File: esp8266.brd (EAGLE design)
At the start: 29.5 x 28.6 mm, 35 parts, among them IC1 74LVC1G08DBV, U1 FT232RL-BASICSSOP, U2 SPX3819M5-L33

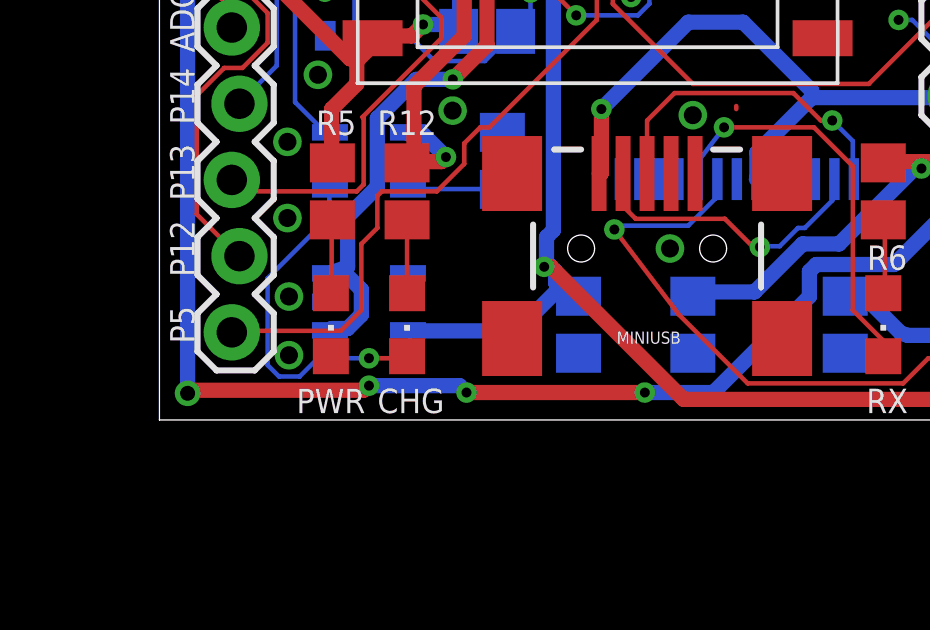
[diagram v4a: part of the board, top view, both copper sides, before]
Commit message: Even less wires and 3 unnecessary vias.
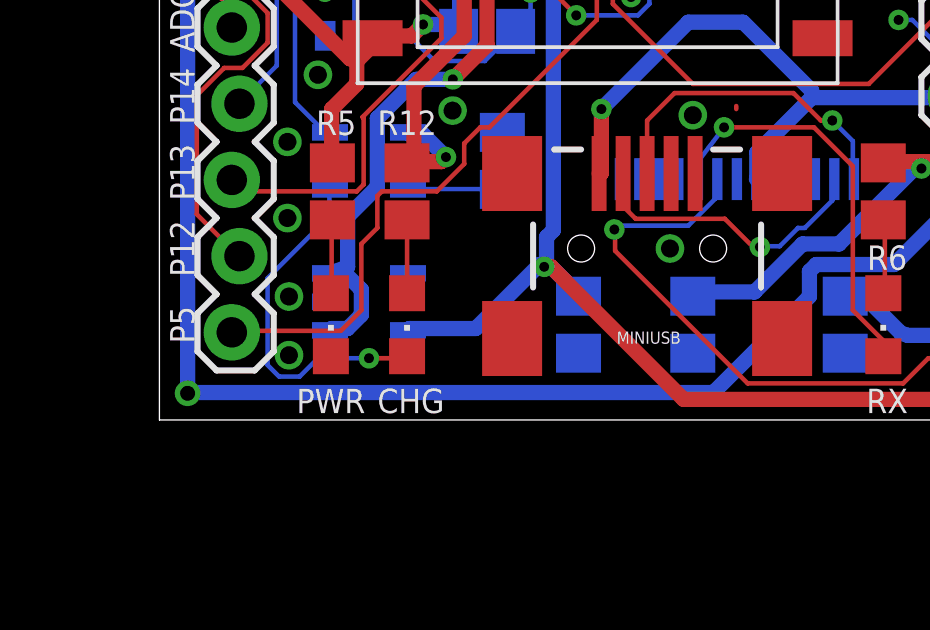
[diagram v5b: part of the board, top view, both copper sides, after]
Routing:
- net VIN: track 73.0 -> 72.8 mm, vias 6 -> 3
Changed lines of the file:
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@@
 <wire x1="11.5062" y1="71.7042" x2="11.5062" y2="72.0852" width="0.508" layer="1"/>
 <wire x1="9.906" y1="70.104" x2="11.5062" y2="71.7042" width="0.508" layer="1"/>
-<wire x1="19.1262" y1="52.3494" x2="18.8976" y2="52.578" width="0.508" layer="16"/>
-<wire x1="25.0698" y1="52.3494" x2="19.1262" y2="52.3494" width="0.508" layer="1"/>
-<wire x1="27.3558" y1="52.3494" x2="25.0698" y2="52.3494" width="0.508" layer="16"/>
 <wire x1="30.5562" y1="55.5498" x2="27.3558" y2="52.3494" width="0.508" layer="16"/>
 <wire x1="30.5562" y1="56.388" x2="30.5562" y2="55.5498" width="0.508" layer="16"/>
@@
 <wire x1="35.2044" y1="58.4454" x2="35.433" y2="58.538" width="0.508" layer="16"/>
 <via x="9.906" y="68.453" extent="1-16" drill="0.3302"/>
-<via x="15.875" y="52.578" extent="1-16" drill="0.3302"/>
-<via x="19.1262" y="52.3494" extent="1-16" drill="0.3302"/>
-<via x="25.0698" y="52.3494" extent="1-16" drill="0.3302"/>
 <via x="9.8298" y="52.324" extent="1-16" drill="0.5"/>
-<wire x1="9.8298" y1="52.3494" x2="9.8298" y2="52.324" width="0.508" layer="1"/>
 <wire x1="9.8298" y1="65.6082" x2="9.8298" y2="52.324" width="0.508" layer="16"/>
-<wire x1="10.0584" y1="52.4256" x2="15.6972" y2="52.4256" width="0.508" layer="1"/>
-<wire x1="15.6972" y1="52.4256" x2="15.875" y2="52.578" width="0.508" layer="1"/>
-<wire x1="10.0584" y1="52.4256" x2="9.8298" y2="52.324" width="0.508" layer="1"/>
-<wire x1="18.8976" y1="52.578" x2="15.875" y2="52.578" width="0.508" layer="16"/>
 <wire x1="9.906" y1="70.104" x2="9.906" y2="68.453" width="0.508" layer="1"/>
 <wire x1="9.906" y1="65.8368" x2="9.906" y2="68.453" width="0.508" layer="16"/>
 <wire x1="9.906" y1="65.8368" x2="9.8298" y2="65.6082" width="0.508" layer="16"/>
+<wire x1="27.3558" y1="52.3494" x2="10.0584" y2="52.3494" width="0.508" layer="16"/>
+<wire x1="10.0584" y1="52.3494" x2="9.8298" y2="52.324" width="0.508" layer="16"/>
 </signal>
 <signal name="DTR">
@@
 <wire x1="14.6304" y1="60.0456" x2="14.6558" y2="60.005" width="0.508" layer="1"/>
 <wire x1="15.9258" y1="64.0842" x2="15.995" y2="64.16" width="0.508" layer="1"/>
-<wire x1="20.955" y1="54.4068" x2="17.2212" y2="54.4068" width="0.508" layer="16"/>
-<wire x1="17.2212" y1="54.4068" x2="17.1751" y2="54.422" width="0.508" layer="16"/>
 <wire x1="22.0218" y1="57.7596" x2="22.0218" y2="67.1322" width="0.508" layer="16"/>
 <wire x1="21.7932" y1="57.531" x2="22.0218" y2="57.7596" width="0.508" layer="16"/>
@@
 <wire x1="34.29" y1="59.817" x2="34.29" y2="60.0456" width="0.508" layer="1"/>
 <wire x1="26.8986" y1="55.7022" x2="26.67" y2="55.56" width="0.508" layer="16"/>
-<wire x1="21.0312" y1="54.6354" x2="22.1742" y2="55.7784" width="0.508" layer="16"/>
-<wire x1="21.0312" y1="54.6354" x2="20.955" y2="54.4068" width="0.508" layer="16"/>
 <via x="34.29" y="59.817" extent="1-16" drill="0.3302"/>
-<wire x1="22.3266" y1="55.626" x2="22.86" y2="55.626" width="0.508" layer="16"/>
-<wire x1="22.86" y1="55.626" x2="22.86" y2="55.56" width="0.508" layer="16"/>
-<wire x1="22.3266" y1="55.626" x2="22.1742" y2="55.7784" width="0.508" layer="16"/>
-<wire x1="22.098" y1="56.388" x2="22.098" y2="56.007" width="0.508" layer="16"/>
-<wire x1="21.7932" y1="56.6928" x2="21.8313" y2="56.6547" width="0.508" layer="16"/>
-<wire x1="21.8313" y1="56.6547" x2="22.098" y2="56.388" width="0.508" layer="16"/>
 <wire x1="21.7932" y1="57.531" x2="21.7932" y2="56.6928" width="0.508" layer="16"/>
-<wire x1="22.098" y1="56.007" x2="22.1742" y2="55.7784" width="0.508" layer="16"/>
 <wire x1="21.9456" y1="56.5404" x2="21.717" y2="56.5404" width="0.508" layer="1"/>
 <wire x1="26.3652" y1="52.1208" x2="21.9456" y2="56.5404" width="0.508" layer="1"/>
@@
 <wire x1="36.7284" y1="59.055" x2="36.7284" y2="52.8828" width="0.508" layer="1"/>
 <wire x1="35.814" y1="59.9694" x2="36.7284" y2="59.055" width="0.508" layer="1"/>
-<wire x1="21.717" y1="56.5404" x2="21.8313" y2="56.6547" width="0.508" layer="16"/>
 <wire x1="35.814" y1="59.9694" x2="35.56" y2="60.005" width="0.508" layer="1"/>
 <via x="21.717" y="56.5404" extent="1-16" drill="0.3302"/>
@@
 <wire x1="18.8976" y1="66.9036" x2="16.383" y2="66.9036" width="0.508" layer="16"/>
 <wire x1="16.383" y1="66.9036" x2="16.317" y2="66.832" width="0.508" layer="16"/>
+<wire x1="19.431" y1="54.483" x2="17.2212" y2="54.483" width="0.508" layer="16"/>
+<wire x1="21.5646" y1="56.6166" x2="19.431" y2="54.483" width="0.508" layer="16"/>
+<wire x1="17.2212" y1="54.483" x2="17.1751" y2="54.422" width="0.508" layer="16"/>
+<wire x1="21.5646" y1="56.6166" x2="21.717" y2="56.5404" width="0.508" layer="16"/>
+<wire x1="21.9456" y1="56.5404" x2="22.86" y2="55.626" width="0.508" layer="16"/>
+<wire x1="22.86" y1="55.626" x2="22.86" y2="55.56" width="0.508" layer="16"/>
+<wire x1="21.9456" y1="56.5404" x2="21.717" y2="56.5404" width="0.508" layer="16"/>
+<wire x1="21.717" y1="56.5404" x2="21.7932" y2="56.6928" width="0.508" layer="16"/>
 </signal>
 <signal name="RXLED">
@@
 <wire x1="33.6804" y1="52.6542" x2="34.5186" y2="53.4924" width="0.1524" layer="1"/>
 <wire x1="28.4988" y1="52.6542" x2="33.6804" y2="52.6542" width="0.1524" layer="1"/>
-<wire x1="26.2128" y1="54.9402" x2="28.4988" y2="52.6542" width="0.1524" layer="1"/>
-<wire x1="24.0538" y1="57.785" x2="26.2128" y2="54.9402" width="0.1524" layer="1"/>
 <wire x1="35.5092" y1="53.4924" x2="35.56" y2="53.56" width="0.1524" layer="1"/>
 <wire x1="27.432" y1="59.436" x2="27.488" y2="59.463" width="0.1524" layer="16"/>
@@
 <wire x1="27.432" y1="58.8264" x2="27.488" y2="59.463" width="0.1524" layer="16"/>
 <wire x1="24.0792" y1="57.8358" x2="24.0538" y2="57.785" width="0.1524" layer="16"/>
+<wire x1="24.0792" y1="57.0738" x2="24.0792" y2="57.7596" width="0.1524" layer="1"/>
+<wire x1="28.4988" y1="52.6542" x2="24.0792" y2="57.0738" width="0.1524" layer="1"/>
+<wire x1="24.0792" y1="57.7596" x2="24.0538" y2="57.785" width="0.1524" layer="1"/>
 </signal>
 <signal name="TXLED">
@@
 <wire x1="32.004" y1="59.5122" x2="32.038" y2="59.463" width="0.1524" layer="16"/>
 <via x="31.3182" y="61.4172" extent="1-16" drill="0.3302"/>
+<wire x1="25.146" y1="61.4172" x2="26.0604" y2="62.3316" width="0.1524" layer="1"/>
+<wire x1="25.146" y1="61.4172" x2="25.146" y2="59.65" width="0.1524" layer="1"/>
 <wire x1="30.9372" y1="61.4172" x2="31.3182" y2="61.4172" width="0.1524" layer="1"/>
 <wire x1="30.0228" y1="62.3316" x2="30.9372" y2="61.4172" width="0.1524" layer="1"/>
 <wire x1="26.0604" y1="62.3316" x2="30.0228" y2="62.3316" width="0.1524" layer="1"/>
-<wire x1="25.146" y1="61.4172" x2="26.0604" y2="62.3316" width="0.1524" layer="1"/>
-<wire x1="25.146" y1="61.4172" x2="25.146" y2="59.65" width="0.1524" layer="1"/>
 </signal>
 <signal name="N$6">

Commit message: I kinda need to stop doing this…
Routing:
- net GND: track 75.1 -> 53.9 mm
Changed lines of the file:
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@@
 <wire x1="28.6512" y1="70.4342" x2="29.4132" y2="68.5038" width="0.1524" layer="16"/>
 <wire x1="30.0228" y1="71.1708" x2="28.6512" y2="70.4342" width="0.1524" layer="1"/>
-<wire x1="35.8902" y1="71.1708" x2="30.0228" y2="71.1708" width="0.1524" layer="1"/>
-<wire x1="36.957" y1="72.2376" x2="35.8902" y2="71.1708" width="0.1524" layer="1"/>
-<wire x1="36.957" y1="78.105" x2="36.957" y2="72.2376" width="0.1524" layer="1"/>
 <wire x1="36.0426" y1="79.0194" x2="36.957" y2="78.105" width="0.1524" layer="1"/>
 <wire x1="29.8704" y1="79.0194" x2="36.0426" y2="79.0194" width="0.1524" layer="1"/>
@@
 <wire x1="15.1638" y1="72.9996" x2="14.7066" y2="73.4568" width="0.1524" layer="1"/>
 <wire x1="17.145" y1="72.9996" x2="15.1638" y2="72.9996" width="0.1524" layer="1"/>
-<wire x1="17.2974" y1="72.8472" x2="17.145" y2="72.9996" width="0.1524" layer="1"/>
-<wire x1="17.2974" y1="67.5132" x2="17.2974" y2="72.8472" width="0.1524" layer="1"/>
 <wire x1="16.8402" y1="67.056" x2="17.2974" y2="67.5132" width="0.1524" layer="1"/>
 <wire x1="14.9352" y1="67.056" x2="16.8402" y2="67.056" width="0.1524" layer="1"/>
@@
 <wire x1="35.2044" y1="63.5508" x2="33.9852" y2="64.77" width="0.1524" layer="16"/>
 <wire x1="36.957" y1="64.3128" x2="36.195" y2="63.5508" width="0.1524" layer="16"/>
-<wire x1="36.957" y1="66.04" x2="36.957" y2="64.3128" width="0.1524" layer="16"/>
-<wire x1="36.957" y1="66.675" x2="36.957" y2="66.04" width="0.1524" layer="1"/>
 <wire x1="37.5666" y1="67.2846" x2="36.957" y2="66.675" width="0.1524" layer="1"/>
 <wire x1="37.5666" y1="69.6468" x2="37.5666" y2="67.2846" width="0.1524" layer="1"/>
@@
 <wire x1="34.0106" y1="71.0438" x2="34.7472" y2="71.0184" width="0.1524" layer="1"/>
 <via x="33.528" y="64.77" extent="1-16" drill="0.3302"/>
-<via x="36.957" y="66.04" extent="1-16" drill="0.3302"/>
+<via x="36.703" y="63.373" extent="1-16" drill="0.3302"/>
 <via x="34.0106" y="71.0438" extent="1-16" drill="0.3302"/>
 <wire x1="28.1178" y1="61.7982" x2="28.1178" y2="61.8998" width="0.1524" layer="1"/>
@@
 <wire x1="11.5062" y1="72.0852" x2="11.557" y2="72.136" width="0.508" layer="1"/>
 <wire x1="35.2044" y1="58.4454" x2="35.433" y2="58.538" width="0.508" layer="16"/>
-<via x="9.906" y="68.453" extent="1-16" drill="0.3302"/>
+<via x="9.9822" y="68.453" extent="1-16" drill="0.3302"/>
 <via x="9.8298" y="52.324" extent="1-16" drill="0.5"/>
 <wire x1="9.8298" y1="65.6082" x2="9.8298" y2="52.324" width="0.508" layer="16"/>
-<wire x1="9.906" y1="70.104" x2="9.906" y2="68.453" width="0.508" layer="1"/>
-<wire x1="9.906" y1="65.8368" x2="9.906" y2="68.453" width="0.508" layer="16"/>
+<wire x1="9.906" y1="70.104" x2="9.9822" y2="68.453" width="0.508" layer="1"/>
+<wire x1="9.906" y1="65.8368" x2="9.9822" y2="68.453" width="0.508" layer="16"/>
 <wire x1="9.906" y1="65.8368" x2="9.8298" y2="65.6082" width="0.508" layer="16"/>
 <wire x1="27.3558" y1="52.3494" x2="10.0584" y2="52.3494" width="0.508" layer="16"/>

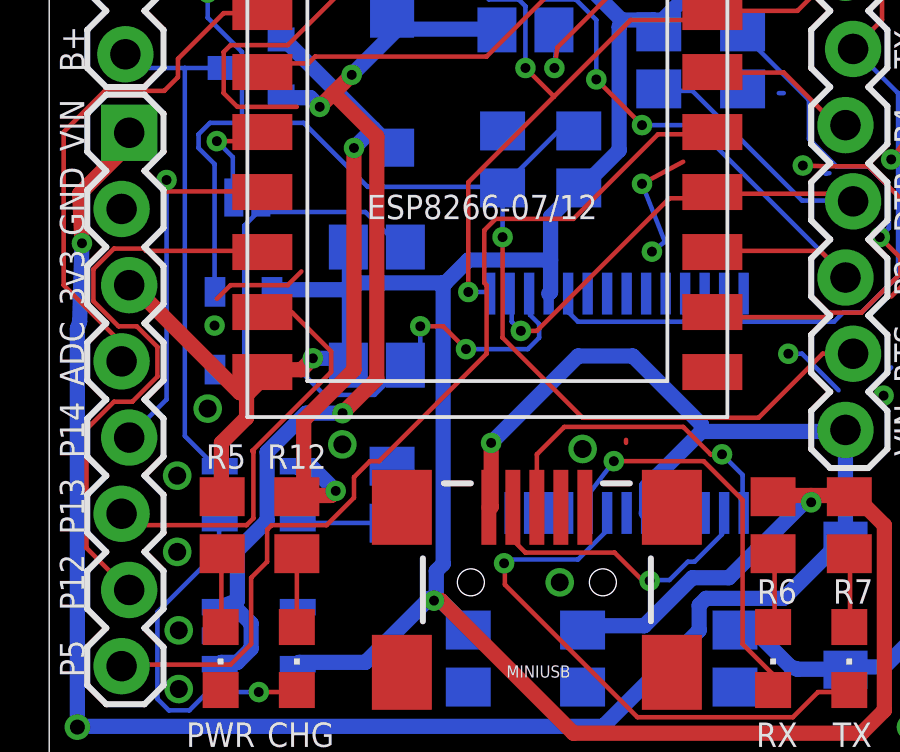
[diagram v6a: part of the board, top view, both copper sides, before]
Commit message: Improve the clarity of the FDTI orientation
This was accomplish by moving the via a to a higher position so that it doesn't interfere with the markings.
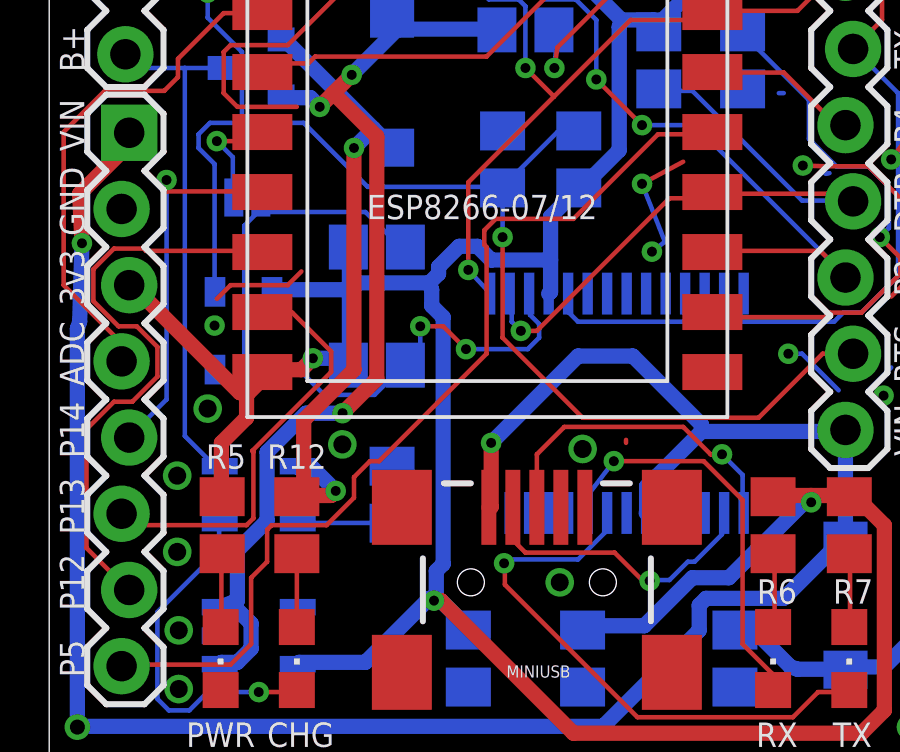
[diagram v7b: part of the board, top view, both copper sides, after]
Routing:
- net 3V3: track 100.1 -> 100.8 mm
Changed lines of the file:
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@@
 <grid distance="0.025" unitdist="inch" unit="inch" style="dots" multiple="1" display="no" altdistance="0.01" altunitdist="inch" altunit="inch"/>
 <layers>
-<layer number="1" name="Top" color="4" fill="1" visible="yes" active="yes"/>
+<layer number="1" name="Top" color="4" fill="1" visible="no" active="yes"/>
 <layer number="16" name="Bottom" color="1" fill="1" visible="yes" active="yes"/>
 <layer number="17" name="Pads" color="2" fill="1" visible="no" active="yes"/>
@@
 <layer number="20" name="Dimension" color="15" fill="1" visible="no" active="yes"/>
 <layer number="21" name="tPlace" color="7" fill="1" visible="no" active="yes"/>
-<layer number="22" name="bPlace" color="7" fill="1" visible="no" active="yes"/>
+<layer number="22" name="bPlace" color="7" fill="1" visible="yes" active="yes"/>
 <layer number="23" name="tOrigins" color="15" fill="1" visible="no" active="yes"/>
-<layer number="24" name="bOrigins" color="15" fill="1" visible="no" active="yes"/>
+<layer number="24" name="bOrigins" color="15" fill="1" visible="yes" active="yes"/>
 <layer number="25" name="tNames" color="7" fill="1" visible="no" active="yes"/>
-<layer number="26" name="bNames" color="7" fill="1" visible="no" active="yes"/>
+<layer number="26" name="bNames" color="7" fill="1" visible="yes" active="yes"/>
 <layer number="27" name="tValues" color="7" fill="1" visible="no" active="yes"/>
-<layer number="28" name="bValues" color="7" fill="1" visible="no" active="yes"/>
+<layer number="28" name="bValues" color="7" fill="1" visible="yes" active="yes"/>
 <layer number="29" name="tStop" color="7" fill="3" visible="no" active="yes"/>
-<layer number="30" name="bStop" color="7" fill="6" visible="no" active="yes"/>
+<layer number="30" name="bStop" color="7" fill="6" visible="yes" active="yes"/>
 <layer number="31" name="tCream" color="7" fill="4" visible="no" active="yes"/>
-<layer number="32" name="bCream" color="7" fill="5" visible="no" active="yes"/>
+<layer number="32" name="bCream" color="7" fill="5" visible="yes" active="yes"/>
 <layer number="33" name="tFinish" color="6" fill="3" visible="no" active="yes"/>
-<layer number="34" name="bFinish" color="6" fill="6" visible="no" active="yes"/>
+<layer number="34" name="bFinish" color="6" fill="6" visible="yes" active="yes"/>
 <layer number="35" name="tGlue" color="7" fill="4" visible="no" active="yes"/>
-<layer number="36" name="bGlue" color="7" fill="5" visible="no" active="yes"/>
+<layer number="36" name="bGlue" color="7" fill="5" visible="yes" active="yes"/>
 <layer number="37" name="tTest" color="7" fill="1" visible="no" active="yes"/>
 <layer number="38" name="bTest" color="7" fill="1" visible="no" active="yes"/>
@@
 <contactref element="ESP8266-07/12" pad="15"/>
 <contactref element="U1" pad="1"/>
-<wire x1="22.86" y1="66.8274" x2="23.5458" y2="66.8274" width="0.1524" layer="16"/>
-<wire x1="22.86" y1="70.485" x2="22.86" y2="66.8274" width="0.1524" layer="1"/>
+<wire x1="22.86" y1="67.564" x2="23.5458" y2="66.8274" width="0.1524" layer="16"/>
+<wire x1="22.86" y1="70.485" x2="22.86" y2="67.564" width="0.1524" layer="1"/>
 <wire x1="28.2702" y1="75.8952" x2="25.7175" y2="73.3425" width="0.1524" layer="1"/>
 <wire x1="25.7175" y1="73.3425" x2="22.86" y2="70.485" width="0.1524" layer="1"/>
@@
 <wire x1="31.0134" y1="76.2" x2="31.242" y2="76.4286" width="0.1524" layer="1"/>
 <wire x1="31.0134" y1="76.2" x2="30.995" y2="76.16" width="0.1524" layer="1"/>
-<via x="22.86" y="66.8274" extent="1-16" drill="0.3302"/>
+<via x="22.86" y="67.564" extent="1-16" drill="0.3302"/>
 <wire x1="35.052" y1="77.4192" x2="35.433" y2="77.4192" width="0.1524" layer="1"/>
 <wire x1="33.8328" y1="76.2" x2="35.052" y2="77.4192" width="0.1524" layer="1"/>
@@
 <wire x1="23.7744" y1="69.2658" x2="26.3652" y2="69.2658" width="0.1524" layer="1"/>
 <wire x1="23.3934" y1="68.8848" x2="23.7744" y2="69.2658" width="0.1524" layer="1"/>
-<wire x1="23.3934" y1="67.1322" x2="23.3934" y2="68.8848" width="0.1524" layer="1"/>
-<wire x1="23.4696" y1="67.056" x2="23.3934" y2="67.1322" width="0.1524" layer="1"/>
-<wire x1="23.4696" y1="64.77" x2="23.4696" y2="67.056" width="0.1524" layer="1"/>
+<wire x1="23.3934" y1="68.4022" x2="23.3934" y2="68.8848" width="0.1524" layer="1"/>
+<wire x1="23.4696" y1="68.326" x2="23.3934" y2="68.4022" width="0.1524" layer="1"/>
+<wire x1="23.4696" y1="64.77" x2="23.4696" y2="68.326" width="0.1524" layer="1"/>
 <wire x1="19.8882" y1="61.1886" x2="23.4696" y2="64.77" width="0.1524" layer="1"/>
 <wire x1="19.5834" y1="61.1886" x2="19.8882" y2="61.1886" width="0.1524" layer="1"/>
@@
 <wire x1="25.6032" y1="66.8274" x2="25.538" y2="66.775" width="0.508" layer="16"/>
 <wire x1="26.5176" y1="70.2564" x2="26.543" y2="70.297" width="0.508" layer="16"/>
-<wire x1="22.098" y1="67.1322" x2="22.0218" y2="67.1322" width="0.508" layer="16"/>
-<wire x1="22.0218" y1="67.1322" x2="18.8976" y2="67.1322" width="0.508" layer="16"/>
-<wire x1="22.86" y1="67.8942" x2="22.098" y2="67.1322" width="0.508" layer="16"/>
-<wire x1="25.6032" y1="67.8942" x2="22.86" y2="67.8942" width="0.508" layer="16"/>
 <wire x1="27.8892" y1="71.5518" x2="27.8892" y2="75.6666" width="0.508" layer="16"/>
 <wire x1="26.7462" y1="70.4088" x2="27.8892" y2="71.5518" width="0.508" layer="16"/>
@@
 <wire x1="14.6304" y1="60.0456" x2="14.6558" y2="60.005" width="0.508" layer="1"/>
 <wire x1="15.9258" y1="64.0842" x2="15.995" y2="64.16" width="0.508" layer="1"/>
-<wire x1="22.0218" y1="57.7596" x2="22.0218" y2="67.1322" width="0.508" layer="16"/>
 <wire x1="21.7932" y1="57.531" x2="22.0218" y2="57.7596" width="0.508" layer="16"/>
 <wire x1="35.5092" y1="60.0456" x2="34.29" y2="60.0456" width="0.508" layer="1"/>
@@
 <wire x1="21.9456" y1="56.5404" x2="21.717" y2="56.5404" width="0.508" layer="16"/>
 <wire x1="21.717" y1="56.5404" x2="21.7932" y2="56.6928" width="0.508" layer="16"/>
+<wire x1="23.622" y1="67.8942" x2="25.6032" y2="67.8942" width="0.508" layer="16"/>
+<wire x1="23.1648" y1="68.3514" x2="23.622" y2="67.8942" width="0.508" layer="16"/>
+<wire x1="22.5552" y1="68.3514" x2="23.1648" y2="68.3514" width="0.508" layer="16"/>
+<wire x1="21.8694" y1="67.6656" x2="22.5552" y2="68.3514" width="0.508" layer="16"/>
+<wire x1="21.8694" y1="67.437" x2="21.8694" y2="67.6656" width="0.508" layer="16"/>
+<wire x1="21.5646" y1="67.1322" x2="21.8694" y2="67.437" width="0.508" layer="16"/>
+<wire x1="18.8976" y1="67.1322" x2="21.5646" y2="67.1322" width="0.508" layer="16"/>
+<wire x1="21.6408" y1="66.3702" x2="21.6408" y2="66.9036" width="0.508" layer="16"/>
+<wire x1="22.0218" y1="65.9892" x2="21.6408" y2="66.3702" width="0.508" layer="16"/>
+<wire x1="22.0218" y1="57.7596" x2="22.0218" y2="65.9892" width="0.508" layer="16"/>
+<wire x1="21.6408" y1="66.9036" x2="21.5646" y2="67.1322" width="0.508" layer="16"/>
 </signal>
 <signal name="RXLED">
